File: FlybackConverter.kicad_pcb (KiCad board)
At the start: 2 copper layers, 76.2 x 76.2 mm, 39 parts, among them J1 USB_C_Receptacle_PowerOnly_6P, T1 Transformer_1P_2S, U1 LNK6428K, U2 TPS25820DSST

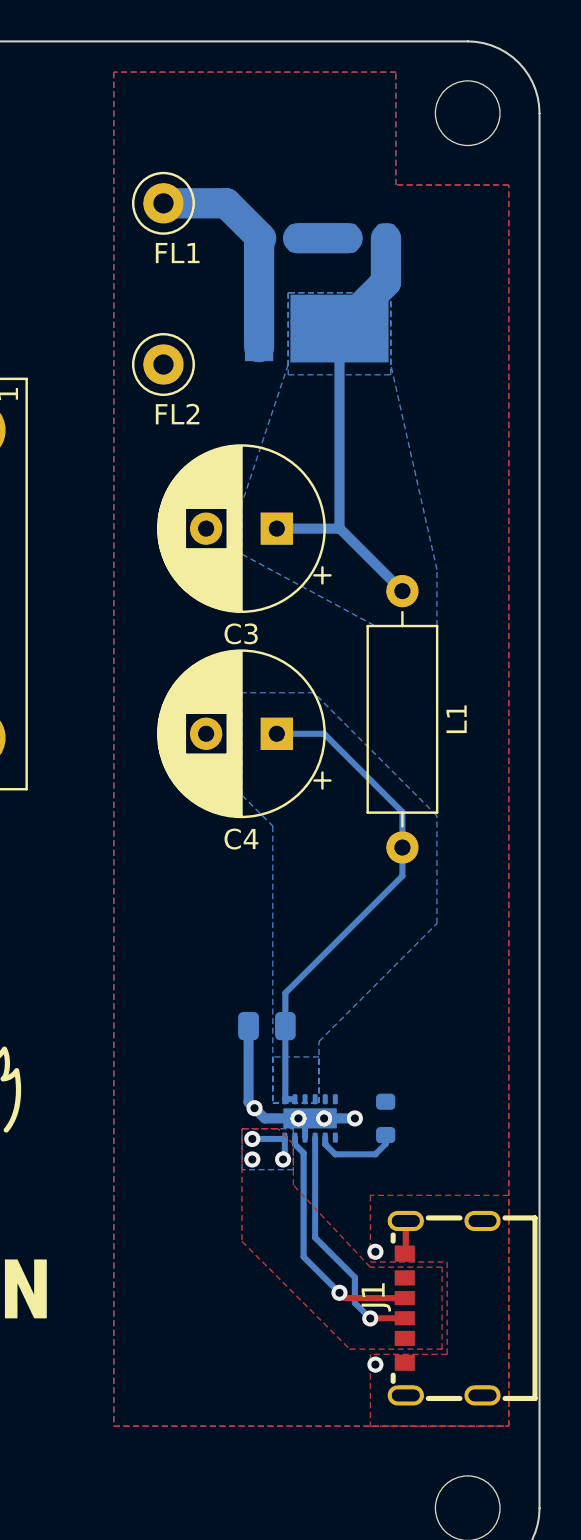
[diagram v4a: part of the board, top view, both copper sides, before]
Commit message: パスコン設置 fix #1
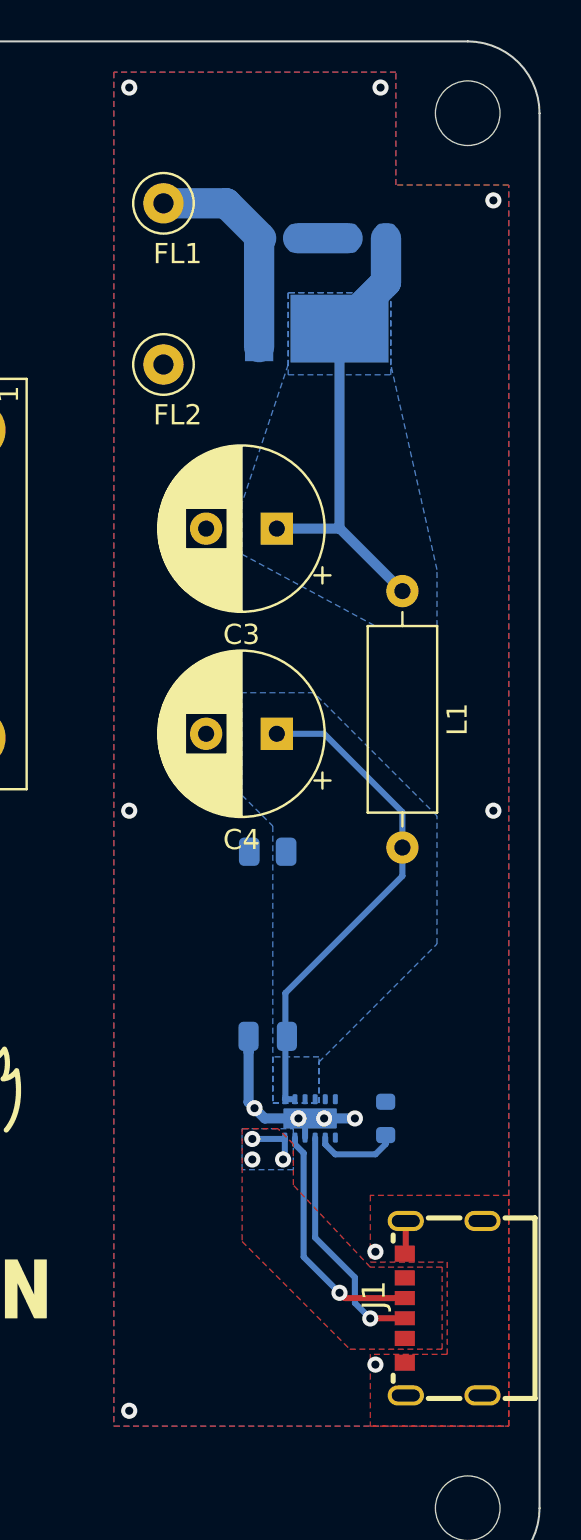
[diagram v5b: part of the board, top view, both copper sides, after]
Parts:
- added C9: 1u, Capacitor_SMD:C_0805_2012Metric, B.Cu at (189.7, 100.1)
- moved R2 8.64 mm to (189.7, 90.9)
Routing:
- net FL2: track 12.3 -> 11.1 mm, vias 6 -> 12
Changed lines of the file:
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@@
   )
   (footprint "Resistor_SMD:R_0805_2012Metric" (layer "B.Cu")
-    (at 189.7025 99.568 180)
+    (at 189.738 90.932 180)
     (descr "Resistor SMD 0805 (2012 Metric), square (rectangular) end terminal, IPC_7351 nominal, (Body size source: IPC-SM-782 page 72, https://www.pcb-3d.com/wordpress/wp-content/uploads/ipc-sm-782a_amendment_1_and_2.pdf), generated with kicad-footprint-generator")
     (tags "resistor")
@@
     )
   )
+  (footprint "Capacitor_SMD:C_0805_2012Metric" (layer "B.Cu")
+    (at 189.738 100.076 180)
+    (descr "Capacitor SMD 0805 (2012 Metric), square (rectangular) end terminal, IPC_7351 nominal, (Body size source: IPC-SM-782 page 76, https://www.pcb-3d.com/wordpress/wp-content/uploads/ipc-sm-782a_amendment_1_and_2.pdf, https://docs.google.com/spreadsheets/d/1BsfQQcO9C6DZCsRaXUlFlo91Tg2WpOkGARC1WS5S8t0/edit?usp=sharing), generated with kicad-footprint-generator")
+    (tags "capacitor")
+    (property "Sheetfile" "FlybackConverter.kicad_sch")
+    (property "Sheetname" "")
+    (property "ki_description" "Unpolarized capacitor")
+    (property "ki_keywords" "cap capacitor")
+    (attr smd)
+    (fp_text reference "C9" (at 0 1.68) (layer "B.SilkS")
+        (effects (font (size 1 1) (thickness 0.15)) (justify mirror))
+    )
+    (fp_text value "1u" (at 0 -1.68) (layer "B.Fab")
+        (effects (font (size 1 1) (thickness 0.15)) (justify mirror))
+    )
+    (fp_text user "${REFERENCE}" (at 0 0) (layer "B.Fab")
+        (effects (font (size 0.5 0.5) (thickness 0.08)) (justify mirror))
+    )
+    (fp_line (start -0.261252 -0.735) (end 0.261252 -0.735)
+      (stroke (width 0.12) (type solid)) (layer "B.SilkS"))
+    (fp_line (start -0.261252 0.735) (end 0.261252 0.735)
+      (stroke (width 0.12) (type solid)) (layer "B.SilkS"))
+    (fp_line (start -1.7 -0.98) (end -1.7 0.98)
+      (stroke (width 0.05) (type solid)) (layer "B.CrtYd"))
+    (fp_line (start -1.7 0.98) (end 1.7 0.98)
+      (stroke (width 0.05) (type solid)) (layer "B.CrtYd"))
+    (fp_line (start 1.7 -0.98) (end -1.7 -0.98)
+      (stroke (width 0.05) (type solid)) (layer "B.CrtYd"))
+    (fp_line (start 1.7 0.98) (end 1.7 -0.98)
+      (stroke (width 0.05) (type solid)) (layer "B.CrtYd"))
+    (fp_line (start -1 -0.625) (end -1 0.625)
+      (stroke (width 0.1) (type solid)) (layer "B.Fab"))
+    (fp_line (start -1 0.625) (end 1 0.625)
+      (stroke (width 0.1) (type solid)) (layer "B.Fab"))
+    (fp_line (start 1 -0.625) (end -1 -0.625)
+      (stroke (width 0.1) (type solid)) (layer "B.Fab"))
+    (fp_line (start 1 0.625) (end 1 -0.625)
+      (stroke (width 0.1) (type solid)) (layer "B.Fab"))
+    (pad "1" smd roundrect (at -0.95 0 180) (size 1 1.45) (layers "B.Cu" "B.Paste" "B.Mask") (roundrect_rratio 0.25)
+      (net 21 "5V") (pintype "passive"))
+    (pad "2" smd roundrect (at 0.95 0 180) (size 1 1.45) (layers "B.Cu" "B.Paste" "B.Mask") (roundrect_rratio 0.25)
+      (net 18 "FL2") (pintype "passive"))
+    (model "${KICAD6_3DMODEL_DIR}/Capacitor_SMD.3dshapes/C_0805_2012Metric.wrl"
+      (offset (xyz 0 0 0))
+      (scale (xyz 1 1 1))
+      (rotate (xyz 0 0 0))
+    )
+  )
   (footprint "Package_TO_SOT_SMD:TO-269AA" (layer "B.Cu")
     (at 155.702 112.268 180)
@@
   (via (at 195.072 110.744) (size 0.8) (drill 0.4) (layers "F.Cu" "B.Cu") (free) (net 18))
   (via (at 191.262 104.14) (size 0.8) (drill 0.4) (layers "F.Cu" "B.Cu") (net 18))
+  (via (at 182.88 53.086) (size 0.8) (drill 0.4) (layers "F.Cu" "B.Cu") (free) (net 18))
   (via (at 195.072 116.332) (size 0.8) (drill 0.4) (layers "F.Cu" "B.Cu") (free) (net 18))
+  (via (at 200.914 88.9) (size 0.8) (drill 0.4) (layers "F.Cu" "B.Cu") (free) (net 18))
   (via (at 189.086051 103.632) (size 0.8) (drill 0.4) (layers "F.Cu" "B.Cu") (net 18))
+  (via (at 200.914 58.674) (size 0.8) (drill 0.4) (layers "F.Cu" "B.Cu") (free) (net 18))
   (via (at 192.532 104.14) (size 0.8) (drill 0.4) (layers "F.Cu" "B.Cu") (net 18))
+  (via (at 182.88 88.9) (size 0.8) (drill 0.4) (layers "F.Cu" "B.Cu") (free) (net 18))
+  (via (at 182.88 118.618) (size 0.8) (drill 0.4) (layers "F.Cu" "B.Cu") (free) (net 18))
   (via (at 194.056 104.14) (size 0.8) (drill 0.4) (layers "F.Cu" "B.Cu") (free) (net 18))
-  (segment (start 188.79 103.335949) (end 188.79 99.568) (width 0.5) (layer "B.Cu") (net 18))
+  (via (at 195.326 53.086) (size 0.8) (drill 0.4) (layers "F.Cu" "B.Cu") (free) (net 18))
+  (segment (start 188.79 100.84) (end 188.788 100.838) (width 0.5) (layer "B.Cu") (net 18))
   (segment (start 192.532 104.14) (end 194.056 104.14) (width 0.5) (layer "B.Cu") (net 18))
+  (segment (start 189.086051 103.632) (end 188.79 103.335949) (width 0.5) (layer "B.Cu") (net 18))
   (segment (start 191.838 104.14) (end 192.532 104.14) (width 0.5) (layer "B.Cu") (net 18))
   (segment (start 191.588 105.09) (end 191.588 104.39) (width 0.3) (layer "B.Cu") (net 18))
@@
   (segment (start 189.086051 103.632) (end 189.594051 104.14) (width 0.5) (layer "B.Cu") (net 18))
   (segment (start 191.588 104.39) (end 191.838 104.14) (width 0.3) (layer "B.Cu") (net 18))
-  (segment (start 189.086051 103.632) (end 188.79 103.335949) (width 0.5) (layer "B.Cu") (net 18))
+  (segment (start 188.79 103.335949) (end 188.79 100.84) (width 0.5) (layer "B.Cu") (net 18))
   (segment (start 189.594051 104.14) (end 191.262 104.14) (width 0.5) (layer "B.Cu") (net 18))
   (segment (start 187.6865 58.819) (end 189.4155 60.548) (width 1.5) (layer "B.Cu") (net 19))
@@
         (xy 189.992 103.378)
         (xy 192.278 103.378)
-        (xy 192.278 100.33)
-        (xy 198.12 94.488)
+        (xy 192.278 101.346)
+        (xy 198.12 95.504)
         (xy 198.12 89.154)
         (xy 192.024 83.058)

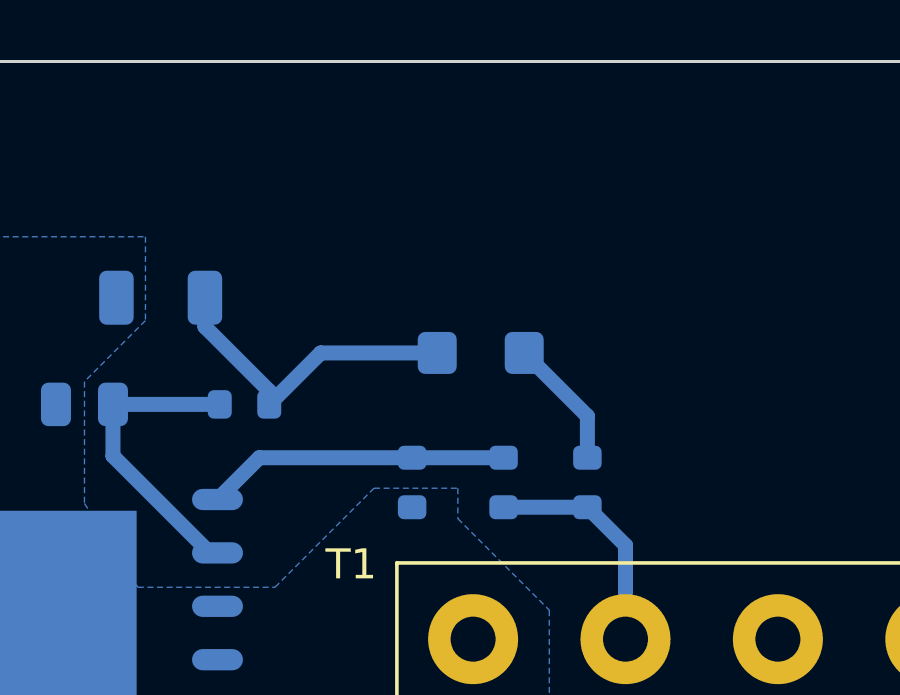
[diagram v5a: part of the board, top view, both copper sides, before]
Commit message: 可変抵抗接続用に配線を引き出せる穴を追加 fix #2
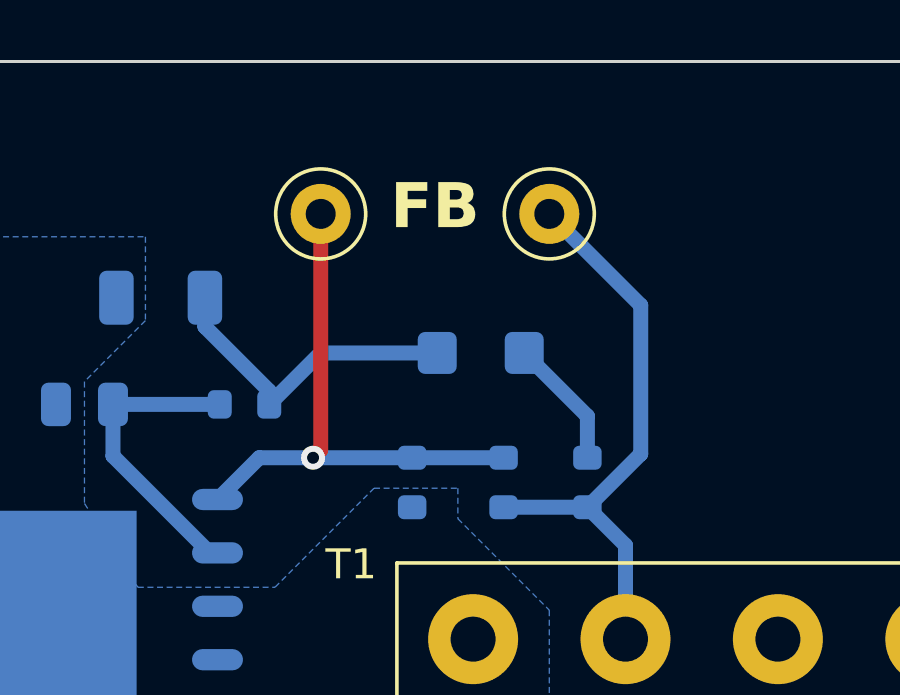
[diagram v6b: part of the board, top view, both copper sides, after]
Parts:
- added TP3: TestPoint, TestPoint:TestPoint_Loop_D1.80mm_Drill1.0mm_Beaded, F.Cu at (162.6, 55.9)
- added TP4: TestPoint, TestPoint:TestPoint_Loop_D1.80mm_Drill1.0mm_Beaded, F.Cu at (154.9, 55.9)
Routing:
- net Net-(T1-SA): track 7.72 -> 19.5 mm
- net Net-(U1-FB): track 10.1 -> 18.3 mm, vias 0 -> 1
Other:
- board text added: "FB"
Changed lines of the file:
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@@
     )
   )
+  (footprint "TestPoint:TestPoint_Loop_D1.80mm_Drill1.0mm_Beaded" (layer "F.Cu")
+    (at 154.94 55.88)
+    (descr "wire loop with bead as test point, loop diameter 1.8mm, hole diameter 1.0mm")
+    (tags "test point wire loop bead")
+    (property "Sheetfile" "FlybackConverter.kicad_sch")
+    (property "Sheetname" "")
+    (property "ki_description" "test point")
+    (property "ki_keywords" "test point tp")
+    (attr through_hole)
+    (fp_text reference "TP4" (at 0.7 2.5) (layer "F.SilkS") hide
+        (effects (font (size 1 1) (thickness 0.15)))
+    )
+    (fp_text value "TestPoint" (at 0 -2.8) (layer "F.Fab")
+        (effects (font (size 1 1) (thickness 0.15)))
+    )
+    (fp_text user "${REFERENCE}" (at 0.7 2.5) (layer "F.Fab")
+        (effects (font (size 1 1) (thickness 0.15)))
+    )
+    (fp_circle (center 0 0) (end 1.5 0)
+      (stroke (width 0.12) (type solid)) (fill none) (layer "F.SilkS"))
+    (fp_circle (center 0 0) (end 1.8 0)
+      (stroke (width 0.05) (type solid)) (fill none) (layer "F.CrtYd"))
+    (fp_line (start -0.9 -0.2) (end 0.9 -0.2)
+      (stroke (width 0.12) (type solid)) (layer "F.Fab"))
+    (fp_line (start -0.9 0.2) (end -0.9 -0.2)
+      (stroke (width 0.12) (type solid)) (layer "F.Fab"))
+    (fp_line (start 0.9 -0.2) (end 0.9 0.2)
+      (stroke (width 0.12) (type solid)) (layer "F.Fab"))
+    (fp_line (start 0.9 0.2) (end -0.9 0.2)
+      (stroke (width 0.12) (type solid)) (layer "F.Fab"))
+    (fp_circle (center 0 0) (end 1.3 0)
+      (stroke (width 0.12) (type solid)) (fill none) (layer "F.Fab"))
+    (pad "1" thru_hole circle (at 0 0) (size 2 2) (drill 1) (layers "*.Cu" "*.Mask")
+      (net 15 "Net-(U1-FB)") (pinfunction "1") (pintype "passive"))
+    (model "${KICAD6_3DMODEL_DIR}/TestPoint.3dshapes/TestPoint_Loop_D1.80mm_Drill1.0mm_Beaded.wrl"
+      (offset (xyz 0 0 0))
+      (scale (xyz 1 1 1))
+      (rotate (xyz 0 0 0))
+    )
+  )
+  (footprint "TestPoint:TestPoint_Loop_D1.80mm_Drill1.0mm_Beaded" (layer "F.Cu")
+    (at 162.56 55.88)
+    (descr "wire loop with bead as test point, loop diameter 1.8mm, hole diameter 1.0mm")
+    (tags "test point wire loop bead")
+    (property "Sheetfile" "FlybackConverter.kicad_sch")
+    (property "Sheetname" "")
+    (property "ki_description" "test point")
+    (property "ki_keywords" "test point tp")
+    (attr through_hole)
+    (fp_text reference "TP3" (at 0.7 2.5) (layer "F.SilkS") hide
+        (effects (font (size 1 1) (thickness 0.15)))
+    )
+    (fp_text value "TestPoint" (at 0 -2.8) (layer "F.Fab")
+        (effects (font (size 1 1) (thickness 0.15)))
+    )
+    (fp_text user "${REFERENCE}" (at 0.7 2.5) (layer "F.Fab")
+        (effects (font (size 1 1) (thickness 0.15)))
+    )
+    (fp_circle (center 0 0) (end 1.5 0)
+      (stroke (width 0.12) (type solid)) (fill none) (layer "F.SilkS"))
+    (fp_circle (center 0 0) (end 1.8 0)
+      (stroke (width 0.05) (type solid)) (fill none) (layer "F.CrtYd"))
+    (fp_line (start -0.9 -0.2) (end 0.9 -0.2)
+      (stroke (width 0.12) (type solid)) (layer "F.Fab"))
+    (fp_line (start -0.9 0.2) (end -0.9 -0.2)
+      (stroke (width 0.12) (type solid)) (layer "F.Fab"))
+    (fp_line (start 0.9 -0.2) (end 0.9 0.2)
+      (stroke (width 0.12) (type solid)) (layer "F.Fab"))
+    (fp_line (start 0.9 0.2) (end -0.9 0.2)
+      (stroke (width 0.12) (type solid)) (layer "F.Fab"))
+    (fp_circle (center 0 0) (end 1.3 0)
+      (stroke (width 0.12) (type solid)) (fill none) (layer "F.Fab"))
+    (pad "1" thru_hole circle (at 0 0) (size 2 2) (drill 1) (layers "*.Cu" "*.Mask")
+      (net 20 "Net-(T1-SA)") (pinfunction "1") (pintype "passive"))
+    (model "${KICAD6_3DMODEL_DIR}/TestPoint.3dshapes/TestPoint_Loop_D1.80mm_Drill1.0mm_Beaded.wrl"
+      (offset (xyz 0 0 0))
+      (scale (xyz 1 1 1))
+      (rotate (xyz 0 0 0))
+    )
+  )
   (footprint "Diode_SMD:D_PowerDI-5" (layer "B.Cu")
     (at 192.174 65.024 180)
@@
     )
   )
+  (gr_text "FB" (at 158.75 55.626) (layer "F.SilkS")
+    (effects (font (size 1.5 1.5) (thickness 0.3) bold))
+  )
   (segment (start 151.384 91.44) (end 151.384 96.184323) (width 1) (layer "B.Cu") (net 1))
   (segment (start 158.640677 103.441) (end 158.640677 101.518323) (width 1) (layer "B.Cu") (net 1))
@@
   (segment (start 139.7 114.3) (end 142.24 116.84) (width 1) (layer "B.Cu") (net 14))
   (segment (start 134.62 114.3) (end 139.7 114.3) (width 1) (layer "B.Cu") (net 14))
+  (segment (start 154.94 63.754) (end 154.94 55.88) (width 0.5) (layer "F.Cu") (net 15))
+  (segment (start 154.686 64.008) (end 154.94 63.754) (width 0.5) (layer "F.Cu") (net 15))
+  (via (at 154.686 64.008) (size 0.8) (drill 0.4) (layers "F.Cu" "B.Cu") (net 15))
   (segment (start 157.988 64.008) (end 161.036 64.008) (width 0.5) (layer "B.Cu") (net 15))
-  (segment (start 152.892 64.008) (end 157.988 64.008) (width 0.5) (layer "B.Cu") (net 15))
+  (segment (start 154.686 64.008) (end 157.988 64.008) (width 0.5) (layer "B.Cu") (net 15))
+  (segment (start 152.892 64.008) (end 154.686 64.008) (width 0.5) (layer "B.Cu") (net 15))
   (segment (start 151.5 65.4) (end 152.892 64.008) (width 0.5) (layer "B.Cu") (net 15))
   (segment (start 134.62 104.08) (end 139.506 108.966) (width 1) (layer "B.Cu") (net 16))
@@
   (segment (start 163.83 65.658) (end 165.1 66.928) (width 0.5) (layer "B.Cu") (net 20))
   (segment (start 165.1 66.928) (end 165.1 70.055) (width 0.5) (layer "B.Cu") (net 20))
+  (segment (start 165.608 58.928) (end 162.56 55.88) (width 0.5) (layer "B.Cu") (net 20))
+  (segment (start 163.83 65.658) (end 165.608 63.88) (width 0.5) (layer "B.Cu") (net 20))
+  (segment (start 165.608 63.88) (end 165.608 58.928) (width 0.5) (layer "B.Cu") (net 20))
   (segment (start 163.83 65.658) (end 161.036 65.658) (width 0.5) (layer "B.Cu") (net 20))
   (segment (start 196.41 92.134) (end 190.615 97.929) (width 0.3) (layer "B.Cu") (net 21))
